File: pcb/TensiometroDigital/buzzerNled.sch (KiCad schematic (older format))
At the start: 7 parts

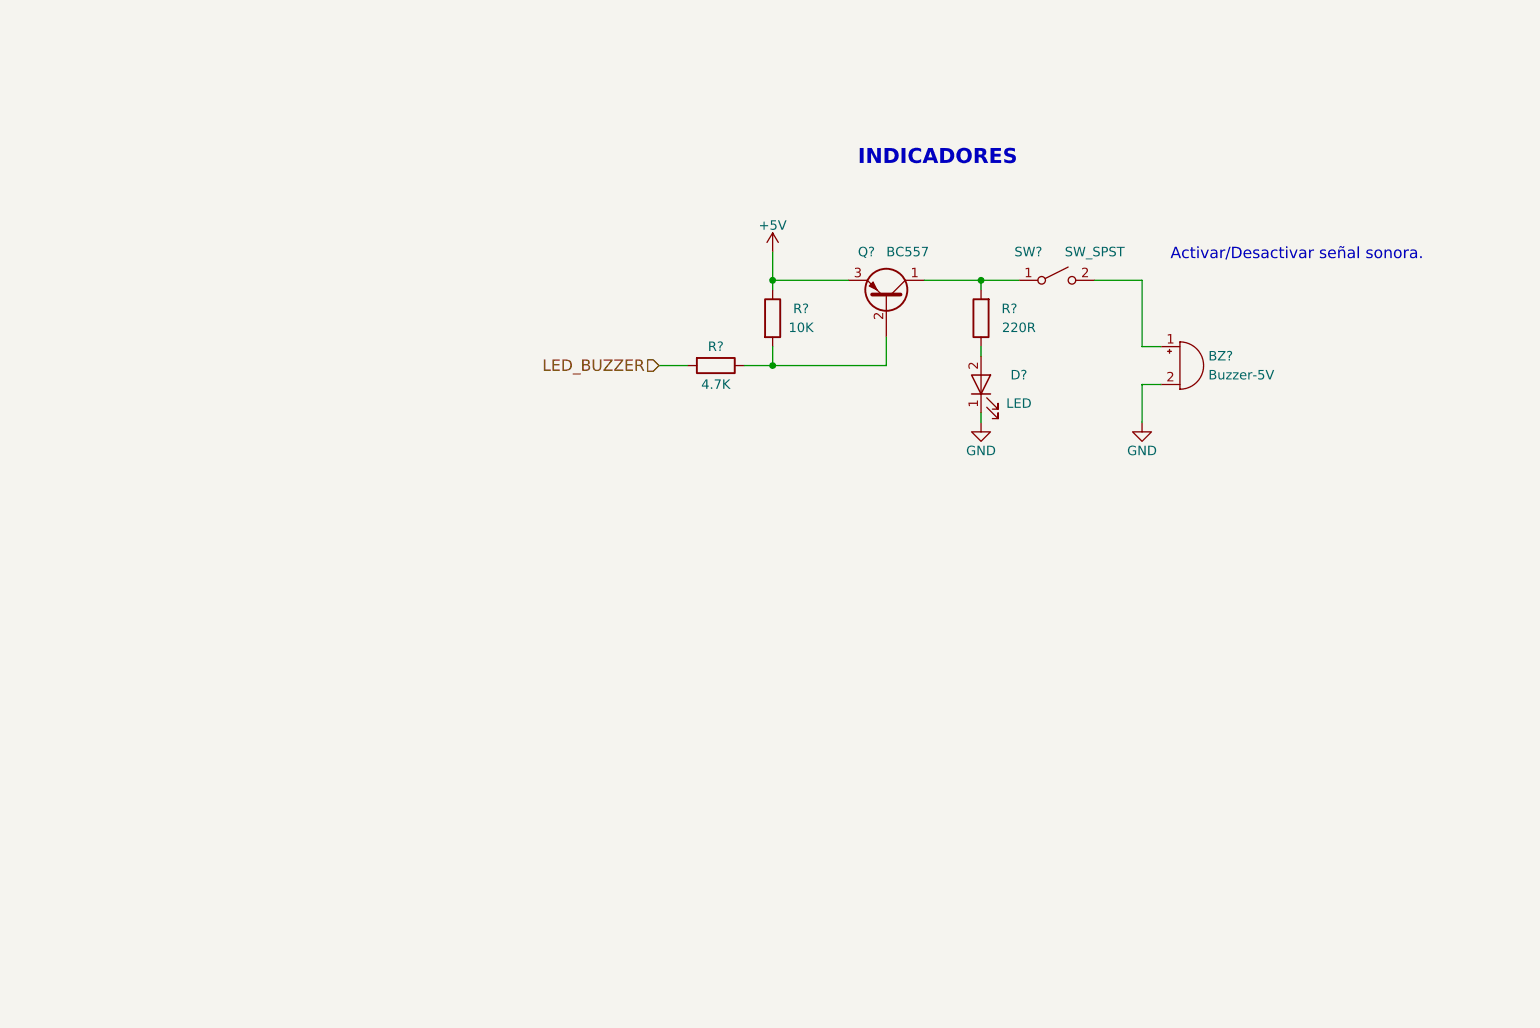
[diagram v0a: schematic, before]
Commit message: Finalizado: SCH, PCB, GABINETE, DRAWINGS. FALTA: GERBERS, BOM e Informe
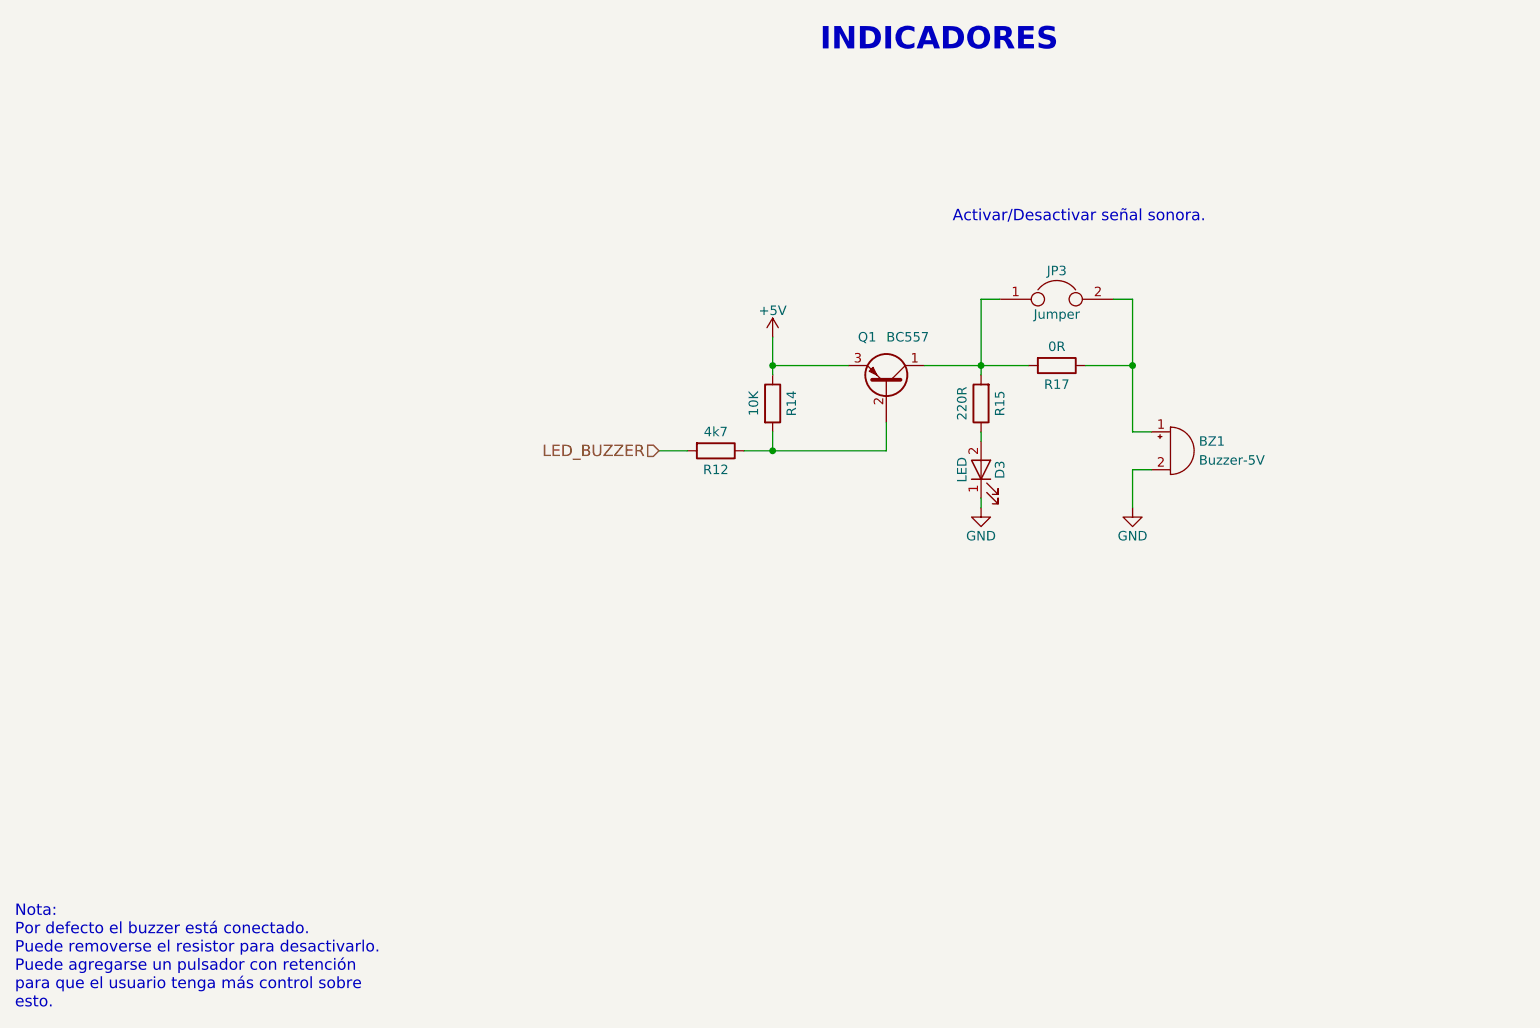
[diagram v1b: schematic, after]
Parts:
- removed SW?: SW_SPST, symbol SW_SPST
- added JP3: Jumper, Socket_Strips:Socket_Strip_Straight_1x02_Pitch2.54mm, symbol Jumper
- added R17: 0R, Resistors_SMD:R_0805_HandSoldering, symbol R
- BZ1: renamed from BZ?; footprint (none) -> Buzzers_Beepers:Buzzer_12x9.5RM7.6; manf# (none) -> CMI-1275C-050
- D3: renamed from D?; footprint (none) -> LEDs:LED_D3.0mm; manf# (none) -> HLMP-K101
- Q1: renamed from Q?; manf# (none) -> BC557
- R12: renamed from R?; value 4.7K -> 4k7; footprint (none) -> Resistors_SMD:R_0805_HandSoldering; manf# (none) -> SG73G2ATTD4701D
- R14: renamed from R?; footprint (none) -> Resistors_SMD:R_0805_HandSoldering; manf# (none) -> SG73G2ATTD1002D
- R15: renamed from R?; footprint (none) -> Resistors_SMD:R_0805_HandSoldering; manf# (none) -> SG73G2ATTD2200D
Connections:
- net at BZ1.1 (-): now also JP3.2, R17.1
- net at Q1.1 (C), R15.2: now also JP3.1, R17.2
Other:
- note added: "Nota:\nPor defecto el buzzer está conectado.\nPuede removerse el resistor para desactivarlo.\nPuede agregarse un pulsador con retención\npara que el usuario tenga más control sobre\nesto."
- moved on the sheet: BZ1, D3, Q1, R12, R14, R15
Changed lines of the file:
@@
 LIBS:lm2940
 LIBS:lm2575
+LIBS:bav199
+LIBS:mpxv5050gp
+LIBS:lm8364
 LIBS:TensiometroDigital-cache
 EELAYER 25 0
@@
 $Descr A4 11693 8268
 encoding utf-8
-Sheet 4 8
-Title ""
-Date ""
-Rev ""
-Comp ""
-Comment1 ""
-Comment2 ""
-Comment3 ""
-Comment4 ""
+Sheet 3 11
+Title "TENSIÓMETRO DIGITAL"
+Date "2018-11-20"
+Rev "A"
+Comp "UTN - FRBA"
+Comment1 "Curso: R1032"
+Comment2 "Leg.: 153204-2"
+Comment3 "Autor: Alegre Mendoza Ezequiel"
+Comment4 "SDR Proyecto Final"
 $EndDescr
 $Comp
-L Buzzer BZ?
+L Buzzer BZ1
 U 1 1 5BBF718D
-P 7050 3700
-F 0 "BZ?" H 7200 3750 50  0000 L CNN
-F 1 "Buzzer-5V" H 7200 3650 50  0000 L CNN
-F 2 "" V 7025 3800 50  0001 C CNN
-F 3 "" V 7025 3800 50  0001 C CNN
-	1    7050 3700
+P 7000 4150
+F 0 "BZ1" H 7150 4200 50  0000 L CNN
+F 1 "Buzzer-5V" H 7150 4100 50  0000 L CNN
+F 2 "Buzzers_Beepers:Buzzer_12x9.5RM7.6" V 6975 4250 50  0001 C CNN
+F 3 "" V 6975 4250 50  0001 C CNN
+F 4 " CMI-1275C-050" H 7000 4150 60  0001 C CNN "manf#"
+	1    7000 4150
 	1    0    0    -1
 $EndComp
 $Comp
-L R R?
+L R R15
 U 1 1 5BBF7208
-P 6000 3450
-F 0 "R?" H 5850 3400 50  0000 C CNN
-F 1 "220R" H 5800 3500 50  0000 C CNN
-F 2 "" V 5930 3450 50  0001 C CNN
-F 3 "" H 6000 3450 50  0001 C CNN
-	1    6000 3450
+P 6000 3900
+F 0 "R15" V 5900 3900 50  0000 C CNN
+F 1 "220R" V 6100 3900 50  0000 C CNN
+F 2 "Resistors_SMD:R_0805_HandSoldering" V 5930 3900 50  0001 C CNN
+F 3 "" H 6000 3900 50  0001 C CNN
+F 4 "SG73G2ATTD2200D" V 6000 3900 60  0001 C CNN "manf#"
+	1    6000 3900
 	-1   0    0    1
 $EndComp
 $Comp
-L GND #PWR?
+L GND #PWR05
 U 1 1 5BBF7298
-P 6000 4000
-F 0 "#PWR?" H 6000 3750 50  0001 C CNN
-F 1 "GND" H 6000 3850 50  0000 C CNN
-F 2 "" H 6000 4000 50  0001 C CNN
-F 3 "" H 6000 4000 50  0001 C CNN
-	1    6000 4000
+P 6000 4450
+F 0 "#PWR05" H 6000 4200 50  0001 C CNN
+F 1 "GND" H 6000 4300 50  0000 C CNN
+F 2 "" H 6000 4450 50  0001 C CNN
+F 3 "" H 6000 4450 50  0001 C CNN
+	1    6000 4450
 	1    0    0    -1
 $EndComp
 $Comp
-L GND #PWR?
+L GND #PWR06
 U 1 1 5BBF72B2
-P 6850 4000
-F 0 "#PWR?" H 6850 3750 50  0001 C CNN
-F 1 "GND" H 6850 3850 50  0000 C CNN
-F 2 "" H 6850 4000 50  0001 C CNN
-F 3 "" H 6850 4000 50  0001 C CNN
-	1    6850 4000
+P 6800 4450
+F 0 "#PWR06" H 6800 4200 50  0001 C CNN
+F 1 "GND" H 6800 4300 50  0000 C CNN
+F 2 "" H 6800 4450 50  0001 C CNN
+F 3 "" H 6800 4450 50  0001 C CNN
+	1    6800 4450
 	1    0    0    -1
 $EndComp
 Wire Wire Line
-	6850 4000 6850 3800
+	6800 4450 6800 4250
 Wire Wire Line
-	6850 3800 6950 3800
+	6800 4250 6900 4250
 Wire Wire Line
-	6000 3600 6000 3650
+	6000 4050 6000 4100
 Wire Wire Line
-	6000 3950 6000 4000
-Text HLabel 4300 3700 0    60   Input ~ 0
+	6000 4400 6000 4450
+Text HLabel 4300 4150 0    60   Input ~ 0
 LED_BUZZER
-Text Notes 5350 2650 0    79   ~ 16
+Text Notes 5150 2050 0    118  ~ 24
 INDICADORES
 $Comp
-L BC557 Q?
+L BC557 Q1
 U 1 1 5BC1217A
-P 5500 3350
-F 0 "Q?" V 5750 3200 50  0000 L CNN
-F 1 "BC557" V 5750 3350 50  0000 L CNN
-F 2 "TO_SOT_Packages_THT:TO-92_Molded_Narrow" H 5700 3275 50  0001 L CIN
-F 3 "" H 5500 3350 50  0001 L CNN
-	1    5500 3350
+P 5500 3800
+F 0 "Q1" V 5750 3650 50  0000 L CNN
+F 1 "BC557" V 5750 3800 50  0000 L CNN
+F 2 "TO_SOT_Packages_THT:TO-92_Molded_Narrow" H 5700 3725 50  0001 L CIN
+F 3 "" H 5500 3800 50  0001 L CNN
+F 4 "BC557" V 5500 3800 60  0001 C CNN "manf#"
+	1    5500 3800
 	0    1    -1   0
 $EndComp
 Wire Wire Line
-	6850 3250 6850 3600
+	6800 4050 6900 4050
 Wire Wire Line
-	6850 3600 6950 3600
+	5500 4150 5500 4000
 Wire Wire Line
-	5500 3700 5500 3550
-Wire Wire Line
-	4750 3700 5500 3700
+	4750 4150 5500 4150
 $Comp
-L R R?
+L R R14
 U 1 1 5BC12359
-P 4900 3450
-F 0 "R?" H 5050 3500 50  0000 C CNN
-F 1 "10K" H 5050 3400 50  0000 C CNN
-F 2 "" V 4830 3450 50  0001 C CNN
-F 3 "" H 4900 3450 50  0001 C CNN
-	1    4900 3450
+P 4900 3900
+F 0 "R14" V 5000 3900 50  0000 C CNN
+F 1 "10K" V 4800 3900 50  0000 C CNN
+F 2 "Resistors_SMD:R_0805_HandSoldering" V 4830 3900 50  0001 C CNN
+F 3 "" H 4900 3900 50  0001 C CNN
+F 4 "SG73G2ATTD1002D " V 4900 3900 60  0001 C CNN "manf#"
+	1    4900 3900
 	1    0    0    -1
 $EndComp
 Wire Wire Line
-	4900 3600 4900 3700
+	4900 4050 4900 4150
 Wire Wire Line
-	4900 3100 4900 3300
+	4900 3550 4900 3750
 Wire Wire Line
-	4900 3250 5300 3250
+	4900 3700 5300 3700
 $Comp
-L +5V #PWR?
+L +5V #PWR07
 U 1 1 5BC123C6
-P 4900 3100
-F 0 "#PWR?" H 4900 2950 50  0001 C CNN
-F 1 "+5V" H 4900 3240 50  0000 C CNN
-F 2 "" H 4900 3100 50  0001 C CNN
-F 3 "" H 4900 3100 50  0001 C CNN
-	1    4900 3100
+P 4900 3550
+F 0 "#PWR07" H 4900 3400 50  0001 C CNN
+F 1 "+5V" H 4900 3690 50  0000 C CNN
+F 2 "" H 4900 3550 50  0001 C CNN
+F 3 "" H 4900 3550 50  0001 C CNN
+	1    4900 3550
 	1    0    0    -1
 $EndComp
-Connection ~ 4900 3250
+Connection ~ 4900 3700
 $Comp
-L R R?
+L R R12
 U 1 1 5BC12413
-P 4600 3700
-F 0 "R?" V 4500 3700 50  0000 C CNN
-F 1 "4.7K" V 4700 3700 50  0000 C CNN
-F 2 "" V 4530 3700 50  0001 C CNN
-F 3 "" H 4600 3700 50  0001 C CNN
-	1    4600 3700
+P 4600 4150
+F 0 "R12" V 4700 4150 50  0000 C CNN
+F 1 "4k7" V 4500 4150 50  0000 C CNN
+F 2 "Resistors_SMD:R_0805_HandSoldering" V 4530 4150 50  0001 C CNN
+F 3 "" H 4600 4150 50  0001 C CNN
+F 4 "SG73G2ATTD4701D" V 4600 4150 60  0001 C CNN "manf#"
+	1    4600 4150
 	0    1    1    0
 $EndComp
 Wire Wire Line
-	4450 3700 4300 3700
-Connection ~ 4900 3700
+	4450 4150 4300 4150
+Connection ~ 4900 4150
 $Comp
-L LED D?
+L LED D3
 U 1 1 5BBF7221
-P 6000 3800
-F 0 "D?" V 6050 3600 50  0000 C CNN
-F 1 "LED" V 5900 3600 50  0000 C CNN
-F 2 "" H 6000 3800 50  0001 C CNN
-F 3 "" H 6000 3800 50  0001 C CNN
-	1    6000 3800
+P 6000 4250
+F 0 "D3" H 6000 4150 50  0000 C CNN
+F 1 "LED" H 6000 4350 50  0000 C CNN
+F 2 "LEDs:LED_D3.0mm" H 6000 4250 50  0001 C CNN
+F 3 "" H 6000 4250 50  0001 C CNN
+F 4 "HLMP-K101" H 6000 4250 60  0001 C CNN "manf#"
+	1    6000 4250
 	0    -1   -1   0
 $EndComp
+Wire Wire Line
+	6550 3700 6800 3700
+Wire Wire Line
+	5700 3700 6250 3700
+Connection ~ 6000 3700
+Text Notes 5850 2950 0    60   ~ 0
+Activar/Desactivar señal sonora.
 $Comp
-L SW_SPST SW?
-U 1 1 5BC13948
-P 6400 3250
-F 0 "SW?" H 6250 3400 50  0000 C CNN
-F 1 "SW_SPST" H 6600 3400 50  0000 C CNN
-F 2 "" H 6400 3250 50  0001 C CNN
-F 3 "" H 6400 3250 50  0001 C CNN
-	1    6400 3250
+L R R17
+U 1 1 5BDC5D1A
+P 6400 3700
+F 0 "R17" V 6500 3700 50  0000 C CNN
+F 1 "0R" V 6300 3700 50  0000 C CNN
+F 2 "Resistors_SMD:R_0805_HandSoldering" V 6330 3700 50  0001 C CNN
+F 3 "" H 6400 3700 50  0001 C CNN
+F 4 "AC0805FR-070RL" V 6400 3700 60  0001 C CNN "manf#"
+	1    6400 3700
+	0    1    1    0
+$EndComp
+Connection ~ 6800 3700
+Text Notes 900  7100 0    60   ~ 0
+Nota:\nPor defecto el buzzer está conectado.\nPuede removerse el resistor para desactivarlo.\nPuede agregarse un pulsador con retención\npara que el usuario tenga más control sobre\nesto.
+Wire Wire Line
+	6000 3350 6000 3750
+Wire Wire Line
+	6800 3350 6800 4050
+$Comp
+L Jumper JP3
+U 1 1 5BE0BC14
+P 6400 3350
+F 0 "JP3" H 6400 3500 50  0000 C CNN
+F 1 "Jumper" H 6400 3270 50  0000 C CNN
+F 2 "Socket_Strips:Socket_Strip_Straight_1x02_Pitch2.54mm" H 6400 3350 50  0001 C CNN
+F 3 "" H 6400 3350 50  0001 C CNN
+	1    6400 3350
 	1    0    0    -1
 $EndComp
 Wire Wire Line
-	6600 3250 6850 3250
+	6700 3350 6800 3350
 Wire Wire Line
-	6000 3300 6000 3250
-Wire Wire Line
-	5700 3250 6200 3250
-Connection ~ 6000 3250
-Text Notes 7000 3150 0    60   ~ 0
-Activar/Desactivar señal sonora.
+	6100 3350 6000 3350
 $EndSCHEMATC
